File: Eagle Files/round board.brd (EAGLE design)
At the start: 15.2 x 15.2 mm, 7 parts

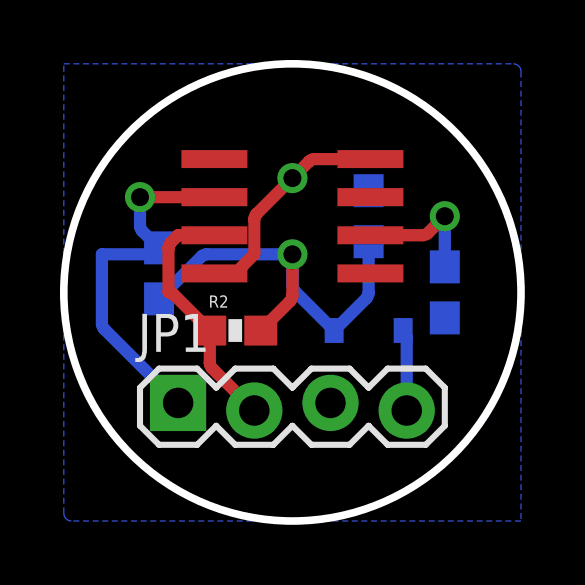
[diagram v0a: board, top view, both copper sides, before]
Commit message: Adjusted silk screen
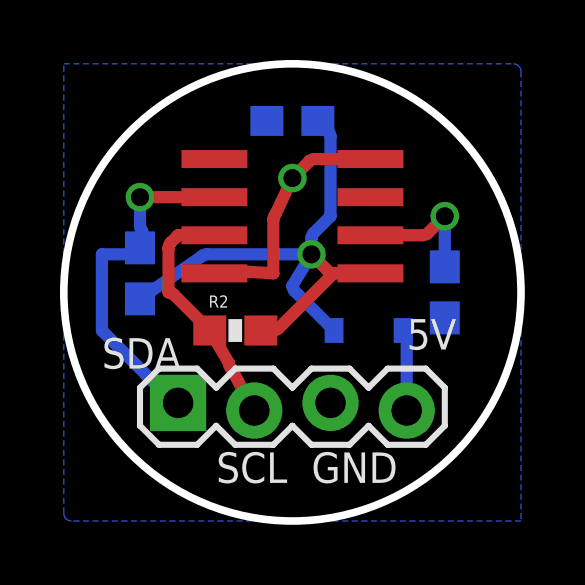
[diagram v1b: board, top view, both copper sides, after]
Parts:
- moved C2 4.07 mm to (12.7, 15.9), turned to 180 degrees
- moved R1 0.64 mm to (7.62, 10.8)
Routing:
- net VDD5V: track 14.5 -> 19.7 mm
- net SDA: track 12.4 -> 11.6 mm
- net GND: track 7.47 -> 8.14 mm
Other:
- board text added: "5V"
- board text added: "GND"
- board text added: "SCL"
- board text added: "SDA"
- board text added: "v1.0"

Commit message: Moved AS5600 footprint to center of board (v1.1)
Removed pull-up resistors
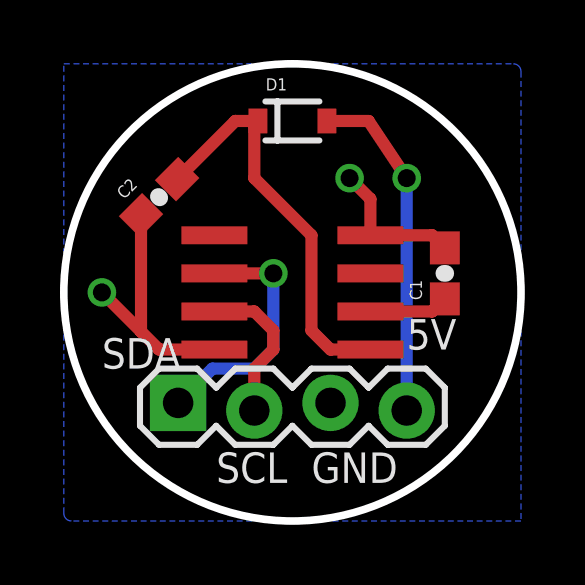
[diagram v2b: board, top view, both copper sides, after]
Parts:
- removed R1, R2: 4.7K, SparkFun-Resistors:0603-RES
- moved D1 7.43 mm to (12.7, 15.9), flipped to the top, turned to 0 degrees
- moved C2 5.12 mm to (8.26, 13.3), flipped to the top, turned to 45 degrees
- moved U$1 2.54 mm to (12.7, 10.2)
- moved C1 0.63 mm to (17.8, 10.8), flipped to the top, turned to 90 degrees
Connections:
- net SCL: no longer R2.1
- net SDA: no longer R1.2
- net VDD5V: no longer R1.1, R2.2
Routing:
- net N$2: track 2.70 -> 11.4 mm, vias 0 -> 1
- net VDD5V: track 19.7 -> 13.5 mm, vias 1 -> 0
- net GND: track 8.14 -> 13.3 mm, vias 1 -> 2
- net SCL: track 8.56 -> 5.16 mm
- net SDA: track 11.6 -> 8.42 mm
- net N$1: track 4.42 -> 2.65 mm, vias 1 -> 0
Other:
- board text added: "v1.1"
- board text removed: "v1.0"
